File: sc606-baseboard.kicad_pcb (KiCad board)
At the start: 6 copper layers, 100 x 80 mm, 419 parts, among them IC1 TPS54561DPRT, IC2 TPS7A0518PDBVT, J1 PJ-202A, J11 WE_632723300011, J13 WE_632723300011, J14 CONMMCX002-SMD-T, J2 WE_68715014522, J3 F52R-1A7H1-11020, J4 46756-1001, J5 U_FL-R-SMT-1_10_, J6 0473460001, J7 DM3AT-SF-PEJM5, J8 693022010811, J9 0473460001, M1 SC606T, Q1 BSS138APW, Q2 BSS138-7-F, Q3 BSS138APW, Q4 BSS138APW, Q5 BSS138APW, Q6 BSS138APW, Q7 BSS138-7-F, Q8 BSS138-7-F, SW1 1X03, U1 AP62301WU-7, U10 NCP163ASN330T1G, U11 EMIF06-MSD02N16, U12 FSUSB30MUX, U13 FT232RQ-REEL, U15 USB57442G, U2 AP62301WU-7, U3 AP62301WU-7, U4 74LVC1G123GN, U5 NTS0102GT, U6 PCA9547BS, U7 LT9611UXC, U8 NTS0102GT, Y1 ABM8G-24.000MHZ-18-D2Y-T, Y2 ABM8G-25.000MHZ-B4Y-T

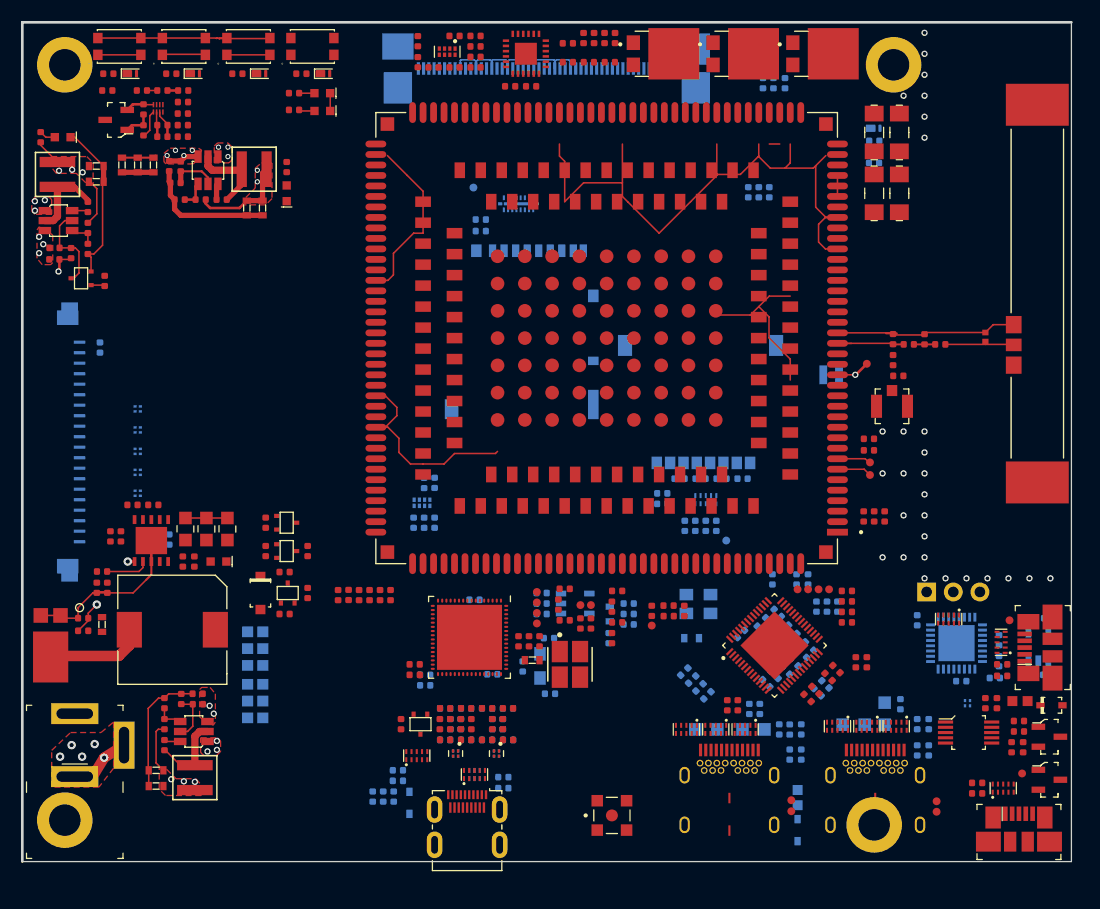
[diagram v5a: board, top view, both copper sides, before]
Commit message: Changed USB flash and debug to USB-C. Prepared place for USB PD. Minor modifications of components position
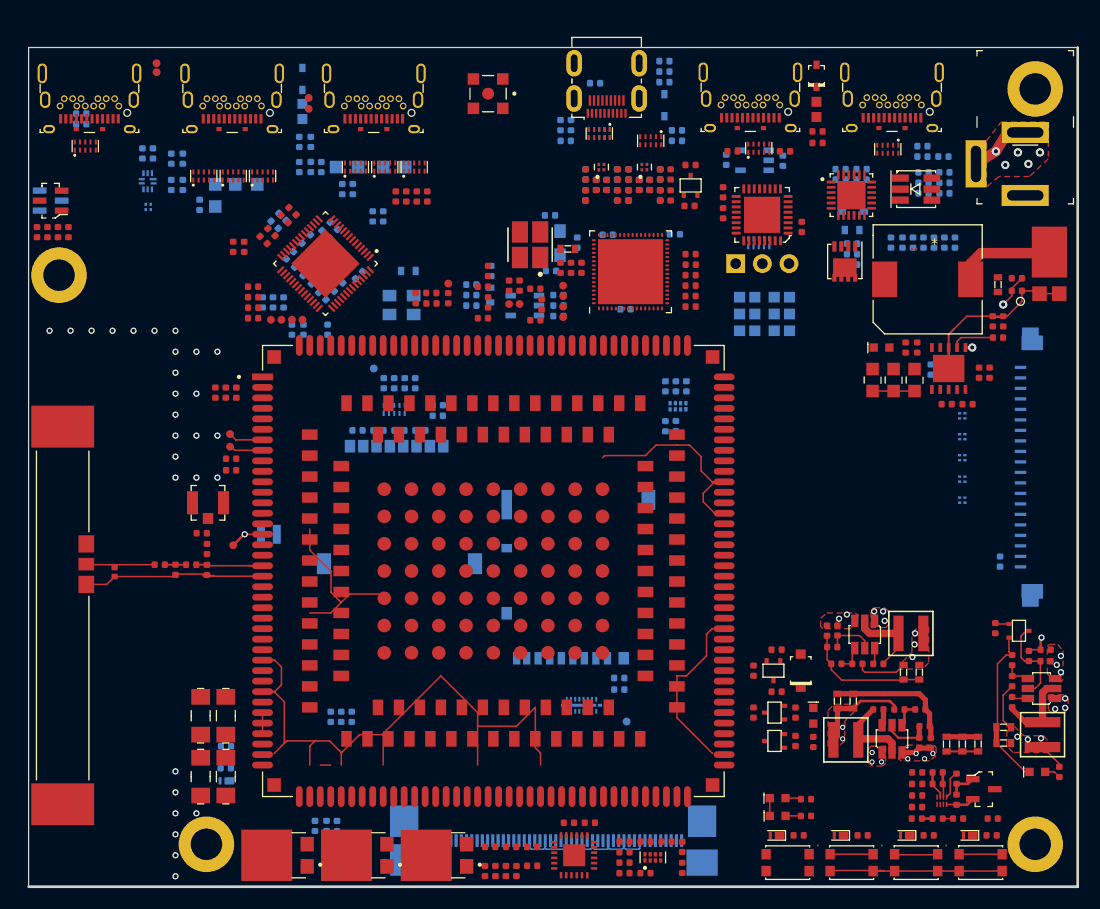
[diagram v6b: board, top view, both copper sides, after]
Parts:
- removed J13: WE_632723300011, sc606-baseboard-footprints:WE_632723300011
- removed TP12, TP20: TP_SMD_0_75MM, sc606-baseboard-footprints:Testpoint_smd_0_75mm
- added C144: C_1u_0402, sc606-baseboard-footprints:0402-cap, B.Cu at (160.9, 56.3)
- added C145: C_1u_0402, sc606-baseboard-footprints:0402-cap, B.Cu at (154.1, 63.1)
- added C146: C_1u_0402, sc606-baseboard-footprints:0402-cap, B.Cu at (154.1, 62.1)
- added C152: C_100n_0402, sc606-baseboard-footprints:0402-cap, B.Cu at (160.8, 52.8)
- added C83: C_4u7_0603, sc606-baseboard-footprints:0603-cap, B.Cu at (154.1, 59.8)
- added C84: C_1u_0603, sc606-baseboard-footprints:0603-cap, B.Cu at (154.1, 56.3)
- added D34: ASMB-TTF0-0A20B, sc606-baseboard-footprints:PLCC6_3.5x3.7mm, F.Cu at (160.2, 55.9)
- added D35: ESD144B1W0201E6327XTSA1, sc606-baseboard-footprints:ESD144B1W0201E6327XTSA1, F.Cu at (160.0, 61.6)
- added D7: PUSB3F96X_PASS, sc606-baseboard-footprints:PUSB3F96X, F.Cu at (157.5, 52.1)
- added D8: PMEG6002EJ,115, sc606-baseboard-footprints:SOD-323F, B.Cu at (154.2, 58.1)
- added J10: E8124-015-01, sc606-baseboard-footprints:USB-C_Female_E8124-015-01, F.Cu at (108.5, 49.2)
- added J12: E8124-015-01, sc606-baseboard-footprints:USB-C_Female_E8124-015-01, F.Cu at (157.9, 49.1)
- added Q9: SQS401EN-T1_BE3, sc606-baseboard-footprints:Vishay_PowerPAK_1212-8_Single, F.Cu at (153.4, 62.8)
- added R142: R_100k_0402, sc606-baseboard-footprints:0402-res, B.Cu at (162.9, 56.3)
- added R143: R_100k_0402, sc606-baseboard-footprints:0402-res, B.Cu at (162.9, 55.3)
- added R144: R_100k_0402, sc606-baseboard-footprints:0402-res, B.Cu at (157.8, 61.0)
- added R145: R_100k_0402, sc606-baseboard-footprints:0402-res, B.Cu at (162.9, 54.3)
- added R146: R_4k7_0402, sc606-baseboard-footprints:0402-res, B.Cu at (158.9, 61.0)
- added R147: R_470R_0402, sc606-baseboard-footprints:0402-res, B.Cu at (155.0, 55.0)
- added R148: R_1k_0402, sc606-baseboard-footprints:0402-res, B.Cu at (153.0, 55.0)
- added R149: R_100k_0402, sc606-baseboard-footprints:0402-res, B.Cu at (155.0, 54.0)
- added R150: R_22k_0402, sc606-baseboard-footprints:0402-res, B.Cu at (153.0, 54.0)
- added R151: R_4k7_0402, sc606-baseboard-footprints:0402-res, B.Cu at (159.9, 61.0)
- added R152: R_4k7_0402, sc606-baseboard-footprints:0402-res, B.Cu at (163.9, 61.0)
- added R153: R_4k7_0402, sc606-baseboard-footprints:0402-res, B.Cu at (161.9, 61.0)
- added R154: R_4k7_0402, sc606-baseboard-footprints:0402-res, B.Cu at (160.9, 61.0)
- added R155: R_4k7_0402, sc606-baseboard-footprints:0402-res, B.Cu at (162.9, 61.0)
- added R156: R_100R_0402, sc606-baseboard-footprints:0402-res, B.Cu at (162.8, 52.8)
- added R157: R_1k1_0402, sc606-baseboard-footprints:0402-res, B.Cu at (160.8, 51.8)
- added R158: R_100R_0402, sc606-baseboard-footprints:0402-res, B.Cu at (160.9, 55.3)
- added R159: R_150R_0402, sc606-baseboard-footprints:0402-res, B.Cu at (160.9, 54.3)
- added R160: R_590R_0402, sc606-baseboard-footprints:0402-res, B.Cu at (154.1, 61.1)
- added U9: FSUSB30UMX, sc606-baseboard-footprints:UMLP-10_1.8x1.4mm, B.Cu at (87.0, 55.1)
- ANT1: footprint antmicro-footprints:47948-0001 -> sc606-baseboard-footprints:47948-0001
- C102, C112, C113, C114, C116, C117, C94, R130, R133, R74, U13: moved to F.Cu
- C108, C109, C110, C140, C141, D23, Q8, R107, R59, R60: moved to B.Cu
- D9: footprint antmicro-footprints:SOD-123 -> sc606-baseboard-footprints:SOD-123
- J11: value WE_632723300011 -> E8124-015-01; footprint sc606-baseboard-footprints:WE_632723300011 -> sc606-baseboard-footprints:USB-C_Female_E8124-015-01
- J6, J9: value 0473460001 -> E8124-015-01; footprint sc606-baseboard-footprints:USB_Micro_B_Female_0473460001 -> sc606-baseboard-footprints:USB-C_Female_E8124-015-01
- R123, R125, R131, R132, R138, R139, R140, R141: footprint antmicro-footprints:0402-res -> sc606-baseboard-footprints:0402-res
- U12: value FSUSB30MUX -> STUSB4500QTR; footprint sc606-baseboard-footprints:MSOP-10_W3mm -> sc606-baseboard-footprints:QFN50P400X400X90-25N
- moved MP2 118.8 mm to (171.6, 118.4), turned to 180 degrees
- moved MP1 115.8 mm to (171.6, 46.4), turned to 180 degrees
- moved R106 114.4 mm to (173.8, 111.5), turned to 270 degrees
- moved S3 113.1 mm to (166.3, 120.1), turned to 0 degrees
- moved R97 111.2 mm to (167.4, 117.5), turned to 180 degrees
- moved D19 110.9 mm to (171.8, 111.5), turned to 0 degrees
- moved Q7 110.0 mm to (77.7, 57.0), turned to 180 degrees
- moved R32 109.3 mm to (167.5, 115.9), turned to 0 degrees
- moved D13 108.1 mm to (165.3, 117.5), turned to 180 degrees
- moved Q8 108.0 mm to (77.7, 57.0)
- moved L3 108.0 mm to (172.2, 107.9), turned to 270 degrees
- moved C109 107.2 mm to (80.6, 48.7)
- moved D20 106.8 mm to (81.0, 51.8)
- moved J1 106.2 mm to (170.6, 53.5), turned to 0 degrees
- moved C110 106.0 mm to (80.6, 49.7)
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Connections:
- D20 pad 1: /USB_flash_debug/USB_FLASH_5V0 -> Net-(D20-Pad1)
- D20 pad 10: /USB_flash_debug/USB_FLASH_5V0 -> Net-(D20-Pad1)
- D20 pad 2: /USB_flash_debug/USB_FLASH_5V0 -> Net-(D20-Pad2)
- D20 pad 4: /USB_flash_debug/USB_FLASH_P -> /USB_flash_debug/USB_FLASH_N
- D20 pad 5: /USB_flash_debug/USB_FLASH_N -> /USB_flash_debug/USB_FLASH_P
- D20 pad 6: /USB_flash_debug/USB_FLASH_N -> /USB_flash_debug/USB_FLASH_P
- D20 pad 7: /USB_flash_debug/USB_FLASH_P -> /USB_flash_debug/USB_FLASH_N
- D20 pad 9: /USB_flash_debug/USB_FLASH_5V0 -> Net-(D20-Pad2)
- D25 pad 1: /USB_HUB_Connectors/USB_C1_D2_N -> /USB_HUB_Connectors/USB_C1_D1_N
- D25 pad 10: /USB_HUB_Connectors/USB_C1_D2_N -> /USB_HUB_Connectors/USB_C1_D1_N
- D25 pad 2: /USB_HUB_Connectors/USB_C1_D2_P -> /USB_HUB_Connectors/USB_C1_D1_P
- D25 pad 4: /USB_HUB_Connectors/USB_C1_D1_N -> /USB_HUB_Connectors/USB_C1_D2_N
- D25 pad 5: /USB_HUB_Connectors/USB_C1_D1_P -> /USB_HUB_Connectors/USB_C1_D2_P
- D25 pad 6: /USB_HUB_Connectors/USB_C1_D1_P -> /USB_HUB_Connectors/USB_C1_D2_P
- D25 pad 7: /USB_HUB_Connectors/USB_C1_D1_N -> /USB_HUB_Connectors/USB_C1_D2_N
- D25 pad 9: /USB_HUB_Connectors/USB_C1_D2_P -> /USB_HUB_Connectors/USB_C1_D1_P
- J11 pad A10: /USB_HUB_Connectors/USB_C1_SS_C_RX2_N -> /USB_HUB_Connectors/USB_C2_SS_C_RX2_N
- J11 pad A11: /USB_HUB_Connectors/USB_C1_SS_C_RX2_P -> /USB_HUB_Connectors/USB_C2_SS_C_RX2_P
- J11 pad A2: /USB_HUB_Connectors/USB_C1_SS_C_TX1_P -> /USB_HUB_Connectors/USB_C2_SS_C_TX1_P
- J11 pad A3: /USB_HUB_Connectors/USB_C1_SS_C_TX1_N -> /USB_HUB_Connectors/USB_C2_SS_C_TX1_N
- J11 pad A5: /USB_HUB_Connectors/USB_C1_CC1 -> /USB_HUB_Connectors/USB_C2_CC1
- J11 pad A6: /USB_HUB_Connectors/USB_C1_D1_P -> /USB_HUB_Connectors/USB_C2_D1_P
- J11 pad A7: /USB_HUB_Connectors/USB_C1_D1_N -> /USB_HUB_Connectors/USB_C2_D1_N
- J11 pad B10: /USB_HUB_Connectors/USB_C1_SS_C_RX1_N -> /USB_HUB_Connectors/USB_C2_SS_C_RX1_N
- J11 pad B11: /USB_HUB_Connectors/USB_C1_SS_C_RX1_P -> /USB_HUB_Connectors/USB_C2_SS_C_RX1_P
- J11 pad B2: /USB_HUB_Connectors/USB_C1_SS_C_TX2_P -> /USB_HUB_Connectors/USB_C2_SS_C_TX2_P
- J11 pad B3: /USB_HUB_Connectors/USB_C1_SS_C_TX2_N -> /USB_HUB_Connectors/USB_C2_SS_C_TX2_N
- J11 pad B5: /USB_HUB_Connectors/USB_C1_CC2 -> /USB_HUB_Connectors/USB_C2_CC2
- J11 pad B6: /USB_HUB_Connectors/USB_C1_D2_P -> /USB_HUB_Connectors/USB_C2_D2_P
- J11 pad B7: /USB_HUB_Connectors/USB_C1_D2_N -> /USB_HUB_Connectors/USB_C2_D2_N
- TP18 pad 1: Net-(J11-PadA8) -> Net-(J10-PadA8)
- TP19 pad 1: Net-(J11-PadB8) -> Net-(J10-PadB8)
- TP23 pad 1: Net-(J13-PadA8) -> Net-(J11-PadA8)
- TP24 pad 1: Net-(J13-PadB8) -> Net-(J11-PadB8)
- U12 pad 1: /USB_flash_debug/USB_FLASH_ENABLE -> /USB-PD/PD_CC1
- U12 pad 10: 3V3_SYS -> GND
- U12 pad 2: USB_HUB_N -> /USB-PD/PD_CC1
- U12 pad 3: /USB_flash_debug/USB_FLASH_P -> (no net)
- U12 pad 4: /USB_flash_debug/SoM_USB_Ferr_D_P -> /USB-PD/PD_CC2
- U12 pad 5: GND -> /USB-PD/PD_CC2
- U12 pad 6: /USB_flash_debug/SoM_USB_Ferr_D_N -> (no net)
- U12 pad 7: /USB_flash_debug/USB_FLASH_N -> STUSB4500_SCL
- U12 pad 8: USB_HUB_P -> STUSB4500_SDA
- U12 pad 9: Net-(R107-Pad1) -> Net-(R157-Pad2)
- U15 pad 1: /USB_HUB_Connectors/USB_C1_D1_P -> /USB_HUB_Connectors/USB_C1_D2_P
- U15 pad 10: /USB_HUB_Connectors/USB_C1_SS_TX2_P -> /USB_HUB_Connectors/USB_C1_SS_TX1_P
- U15 pad 11: /USB_HUB_Connectors/USB_C1_SS_TX2_N -> /USB_HUB_Connectors/USB_C1_SS_TX1_N
- U15 pad 13: /USB_HUB_Connectors/USB_C1_SS_RX2_P -> /USB_HUB_Connectors/USB_C1_SS_RX1_P
- U15 pad 14: /USB_HUB_Connectors/USB_C1_SS_RX2_N -> /USB_HUB_Connectors/USB_C1_SS_RX1_N
- U15 pad 2: /USB_HUB_Connectors/USB_C1_D1_N -> /USB_HUB_Connectors/USB_C1_D2_N
- U15 pad 3: /USB_HUB_Connectors/USB_C1_SS_TX1_P -> /USB_HUB_Connectors/USB_C1_SS_TX2_P
- U15 pad 4: /USB_HUB_Connectors/USB_C1_SS_TX1_N -> /USB_HUB_Connectors/USB_C1_SS_TX2_N
- U15 pad 6: /USB_HUB_Connectors/USB_C1_SS_RX1_P -> /USB_HUB_Connectors/USB_C1_SS_RX2_P
- U15 pad 7: /USB_HUB_Connectors/USB_C1_SS_RX1_N -> /USB_HUB_Connectors/USB_C1_SS_RX2_N
- U15 pad 8: /USB_HUB_Connectors/USB_C1_D2_P -> /USB_HUB_Connectors/USB_C1_D1_P
- U15 pad 9: /USB_HUB_Connectors/USB_C1_D2_N -> /USB_HUB_Connectors/USB_C1_D1_N

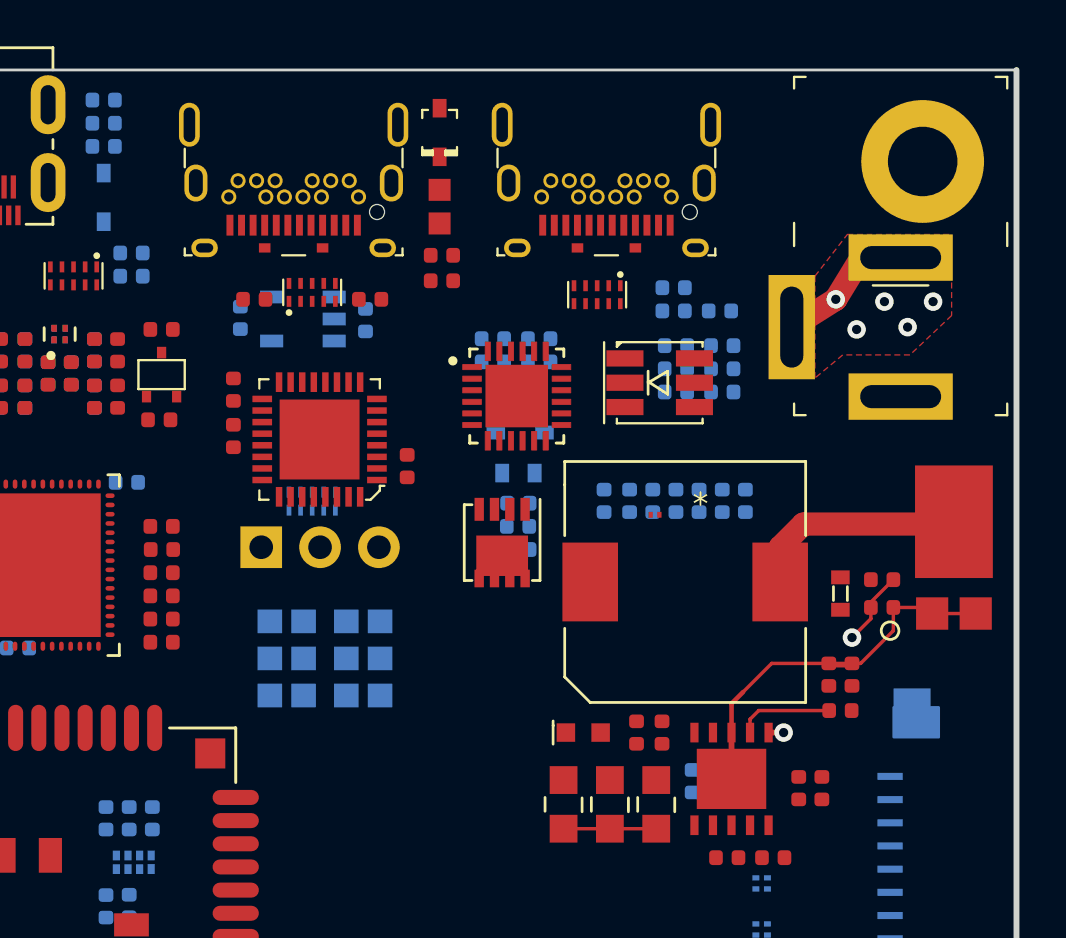
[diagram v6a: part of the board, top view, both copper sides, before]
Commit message: Connected USB-PD and power select chip
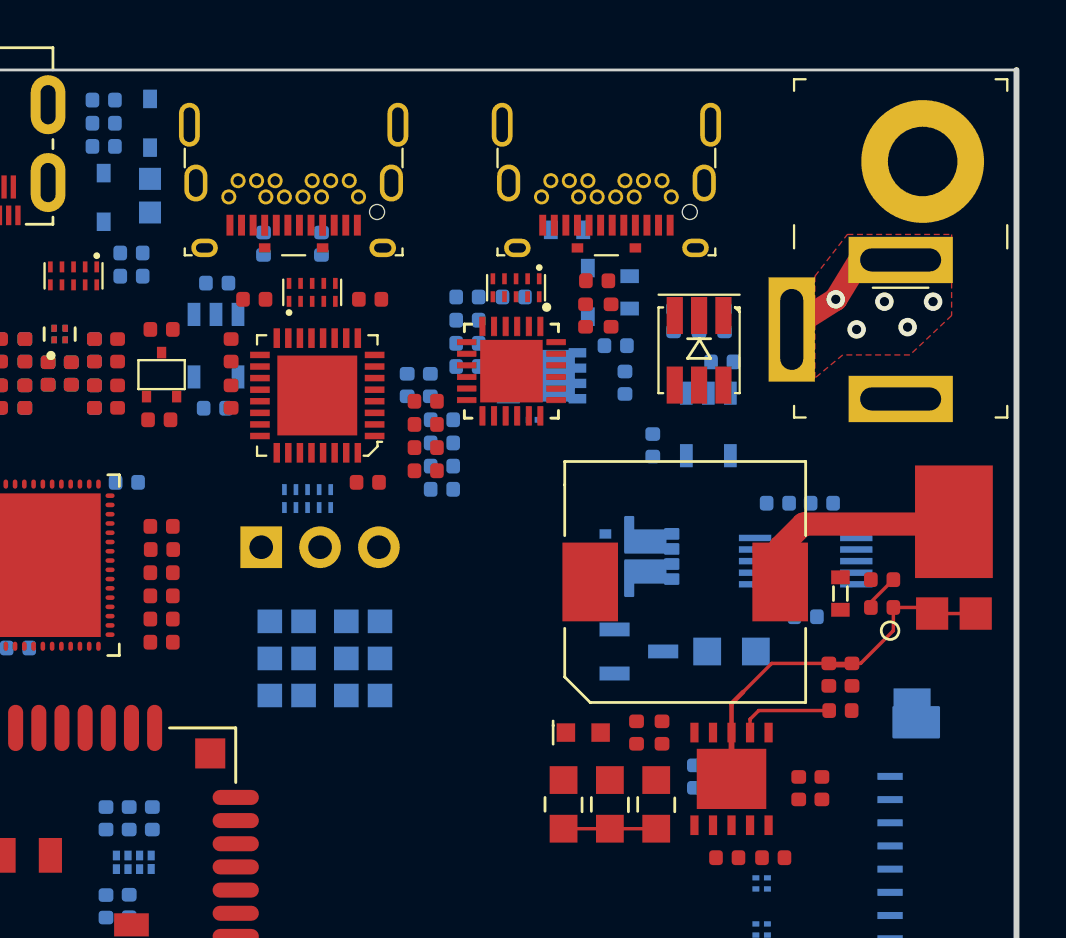
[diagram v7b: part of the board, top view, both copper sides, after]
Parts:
- added C153: C_100u_0805, antmicro-footprints:0805-cap, B.Cu at (163.3, 67.5)
- added C154: C_2u2_0402, sc606-baseboard-footprints:0402-cap, B.Cu at (162.9, 55.0)
- added C155: C_1u_0402, sc606-baseboard-footprints:0402-cap, B.Cu at (159.9, 58.6)
- added IC3: TPS7A0518PDBVT, sc606-baseboard-footprints:SOT-23-5, B.Cu at (162.3, 57.7)
- added Q10: BSS84, antmicro-footprints:SOT-23-3, B.Cu at (159.3, 67.5)
- added Q11: Si7223DN, sa800u-baseboard-hw-footprints:PowerPak-1212, B.Cu at (159.3, 63.4)
- added R161: R_220k_0402, antmicro-footprints:0402-res, B.Cu at (166.5, 66.0)
- added R163: R_24k9_0402, antmicro-footprints:0402-res, B.Cu at (165.3, 61.1)
- added R164: R_180k_0402, antmicro-footprints:0402-res, B.Cu at (167.2, 61.1)
- added U14: LTC4416IMS-1, antmicro-footprints:MSOP-10_MS, B.Cu at (166.5, 63.6)
- C142, C143, D22, D35, FB1, Q9: moved to B.Cu
- C144, C145, C146, R142, R143, R144, R145: moved to F.Cu
- moved R145 13.9 mm to (150.1, 59.7)
- moved R152 13.6 mm to (150.8, 57.5), turned to 180 degrees
- moved R153 13.6 mm to (149.3, 56.0)
- moved R143 13.2 mm to (150.1, 58.7)
- moved R142 12.9 mm to (150.1, 57.7)
- moved FB1 12.5 mm to (138.2, 47.8)
- moved D22 12.5 mm to (138.2, 44.7)
- moved R155 12.1 mm to (150.8, 60.5), turned to 180 degrees
- moved R154 11.7 mm to (150.3, 56.0)
- moved C146 11.1 mm to (157.5, 51.5)
- moved R160 11.1 mm to (161.9, 53.2), turned to 270 degrees
- moved R156 10.9 mm to (151.9, 53.2)
- moved C145 10.9 mm to (158.1, 53.0), turned to 270 degrees
- moved C83 10.7 mm to (156.2, 49.3), turned to 180 degrees
- moved R157 9.53 mm to (151.9, 55.2), turned to 180 degrees
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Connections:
- C17 pad 1: VCC -> VDD
- C18 pad 1: VCC -> VDD
- C19 pad 1: VCC -> VDD
- D35 pad 1: (no net) -> PD_VDD
- D7 pad 2: /USB-PD/PD_CC2 -> Net-(D7-Pad2)
- D7 pad 5: Net-(D7-Pad5) -> /USB-PD/PD_CC2
- D7 pad 6: Net-(D7-Pad5) -> /USB-PD/PD_CC2
- D7 pad 9: /USB-PD/PD_CC2 -> Net-(D7-Pad2)
- IC1 pad 2: VCC -> VDD
- J1 pad 1: VCC -> AUX_VDD
- R4 pad 1: VCC -> VDD
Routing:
- net Net-(IC1-Pad6): track 9.21 -> 1.60 mm, vias 2 -> 0
- net VDD: track 0.00 -> 4.00 mm
- net VCC: track 4.00 -> 0.00 mm
